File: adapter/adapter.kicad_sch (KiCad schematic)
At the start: 32 parts, among them J1 Serial, J10 Ribbon, J11 Ribbon, J12 Ribbon, J13 serial, J14 serial, J2 Serial, J3 battery charge, J4 RGB, J5 RGB, J6 battery charge, J7 trackball, J8 trackball, J9 Ribbon, SW1 SW_SPST, SW2 SW_SPST, SW3 SW_SPDT, SW4 SW_SPDT, U1 eliteC, U2 eliteC

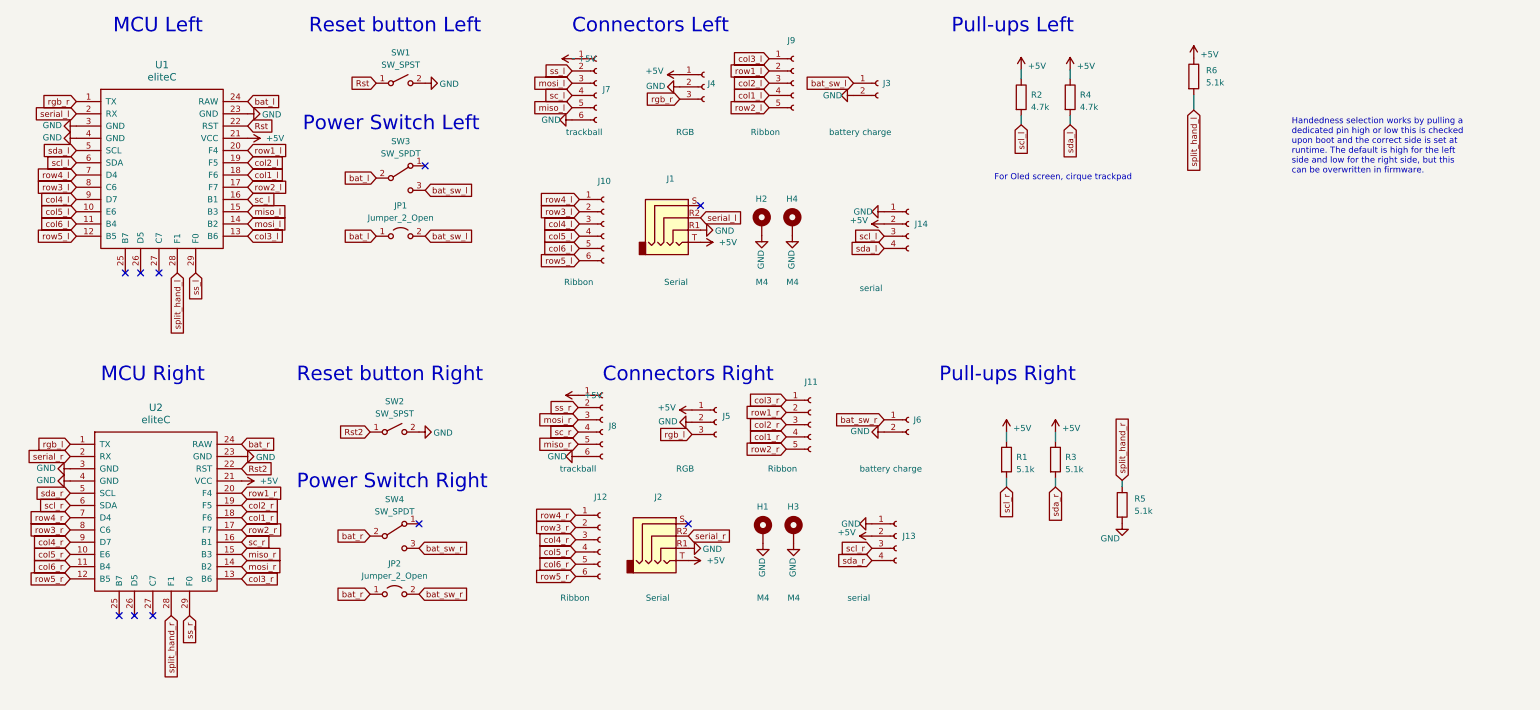
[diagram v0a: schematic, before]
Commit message: Remove all of the components except matrix pins and add nice!nano schematic from github
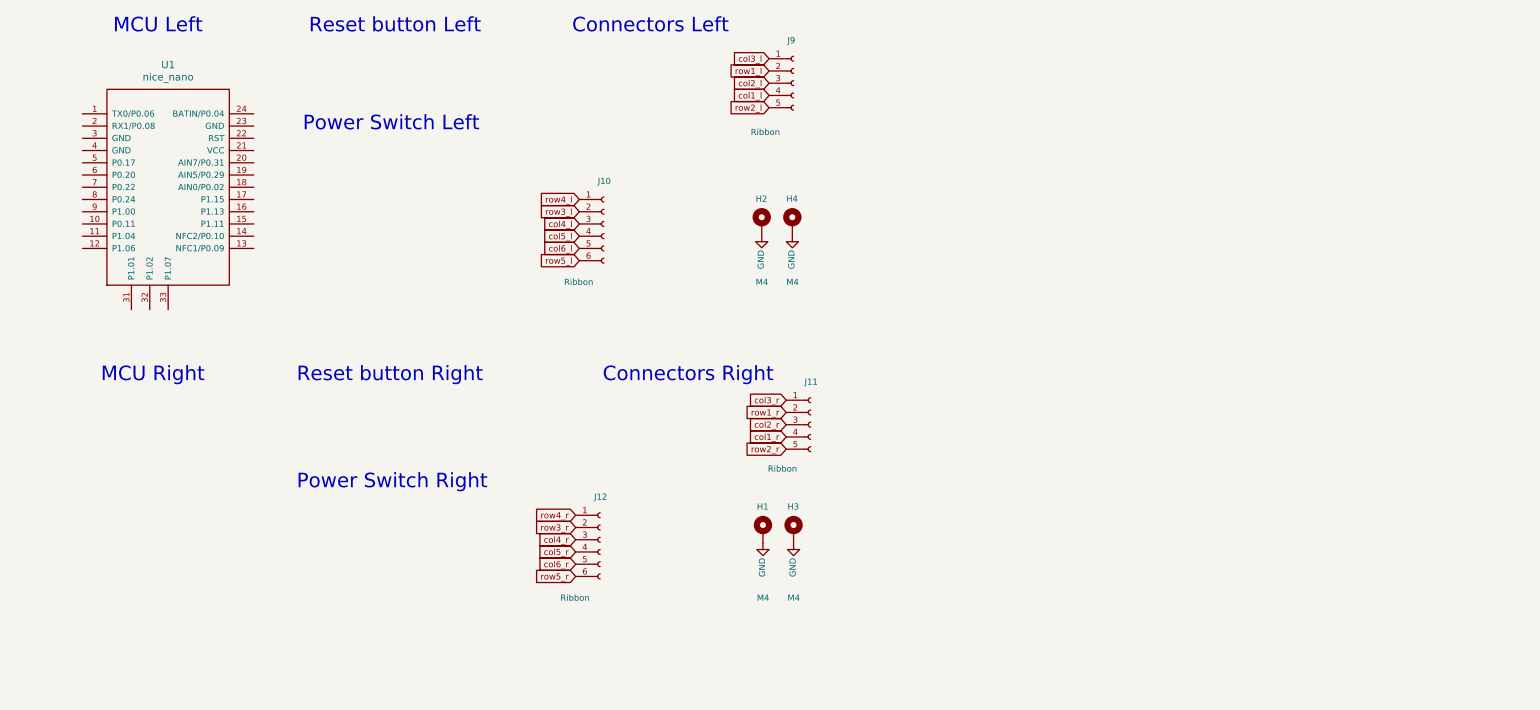
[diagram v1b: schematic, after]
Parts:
- removed J1, J2: Serial, Library:Jack_3.5mm_PJ320E_Horizontal, symbol Connector:AudioJack4
- removed J13, J14: serial, Library:PinHeader_1x04_P2.54mm_Vertical, symbol Connector:Conn_01x04_Female
- removed J3, J6: battery charge, Library:PinHeader_1x02_P2.54mm_Vertical, symbol Connector:Conn_01x02_Female
- removed J4, J5: RGB, Library:header1x03, symbol Connector:Conn_01x03_Female
- removed J7, J8: trackball, Library:6_PinHeader, symbol Connector:Conn_01x06_Female
- removed JP1, JP2: Jumper_2_Open, Library:power_switch_jumper, symbol Jumper:Jumper_2_Open
- removed R1, R3, R5, R6: 5.1k, Library:R_1206_handsolder, symbol Device:R
- removed R2, R4: 4.7k, Library:R_1206_handsolder, symbol Device:R
- removed SW1, SW2: SW_SPST, Library:PushSwitch, symbol Switch:SW_SPST
- removed SW3, SW4: SW_SPDT, Library:SW_SPDT+H-MSK12C01_hor(7pin_SMD), symbol Switch:SW_SPDT
- removed U1, U2: eliteC, Library:Elite-C, symbol elite-C:eliteC
- added U1: nice_nano, Library:nice_nano, symbol nice_nano:nice_nano
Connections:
- no-connect marks 10 -> 0
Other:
- note removed: "For Oled screen, cirque trackpad"
- note removed: "Handedness selection works by pulling a dedicated pin high or low this is checked upon boot and the correct side is set at runtime. The default is high for the left side and low for the right side, but this can be overwritten in firmware."
- note removed: "Pull-ups Left"
- note removed: "Pull-ups Right"
